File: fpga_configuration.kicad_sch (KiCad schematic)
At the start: 53 parts, among them IC1 ECP5-BGA256, J10 TC_SWD, J6 MCU_SWD, U6 ATSAMD11, U7 W25Q32JVSS

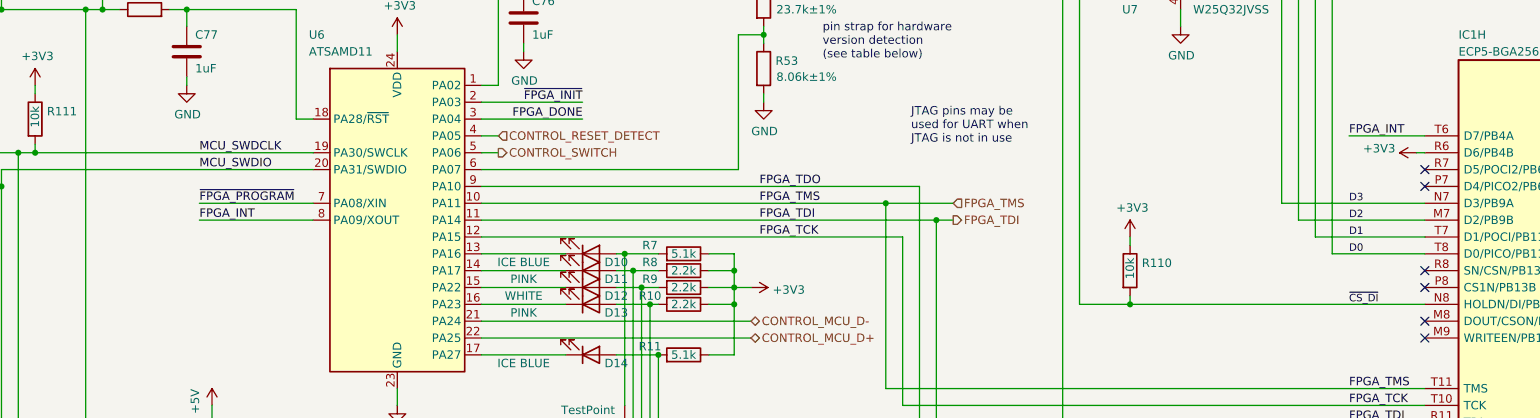
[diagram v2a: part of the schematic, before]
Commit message: Rename FPGA_INT to FPGA_ADV
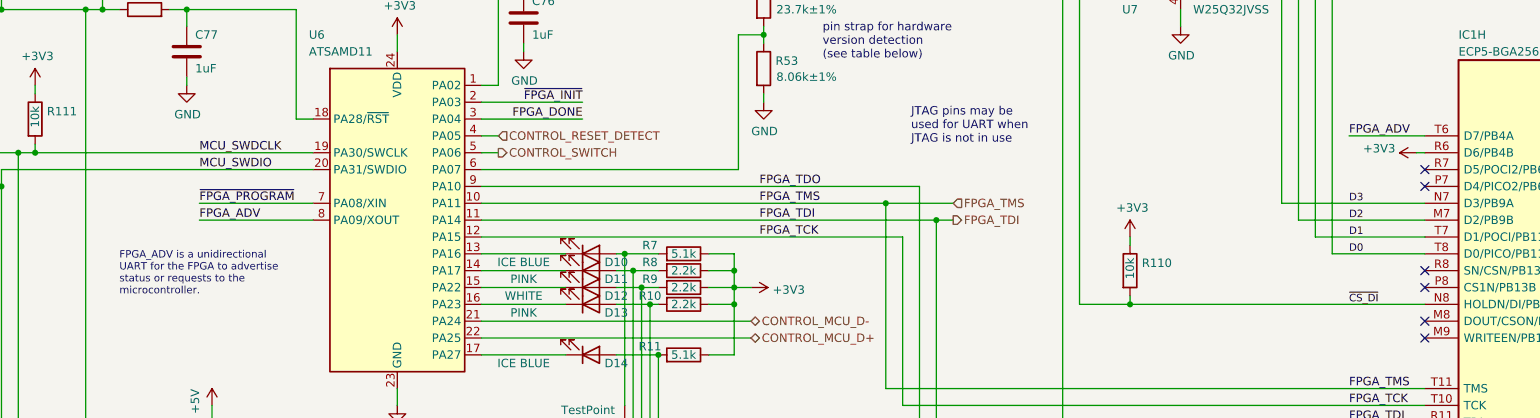
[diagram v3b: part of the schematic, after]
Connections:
- net FPGA_INT renamed FPGA_ADV
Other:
- note added: "FPGA_ADV is a unidirectional UART for the FPGA to advertise status or requests to the microcontroller."
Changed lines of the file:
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@@
     (effects (font (size 1.27 1.27)) (justify left bottom))
+  )
+  (text "FPGA_ADV is a unidirectional\nUART for the FPGA to advertise\nstatus or requests to the\nmicrocontroller."
+    (at 50.8 91.44 0)
+    (effects (font (size 1.1176 1.1176)) (justify left bottom))
   )
   (text "1.2" (at 135.89 182.88 0)
@@
     (effects (font (size 1.27 1.27)) (justify right bottom))
   )
-  (label "FPGA_INT" (at 236.22 67.31 0)
+  (label "FPGA_ADV" (at 236.22 67.31 0)
     (effects (font (size 1.27 1.27)) (justify left bottom))
   )
@@
     (effects (font (size 1.27 1.27)) (justify left bottom))
   )
-  (label "FPGA_INT" (at 62.865 80.01 0)
+  (label "FPGA_ADV" (at 62.865 80.01 0)
     (effects (font (size 1.27 1.27)) (justify left bottom))
   )

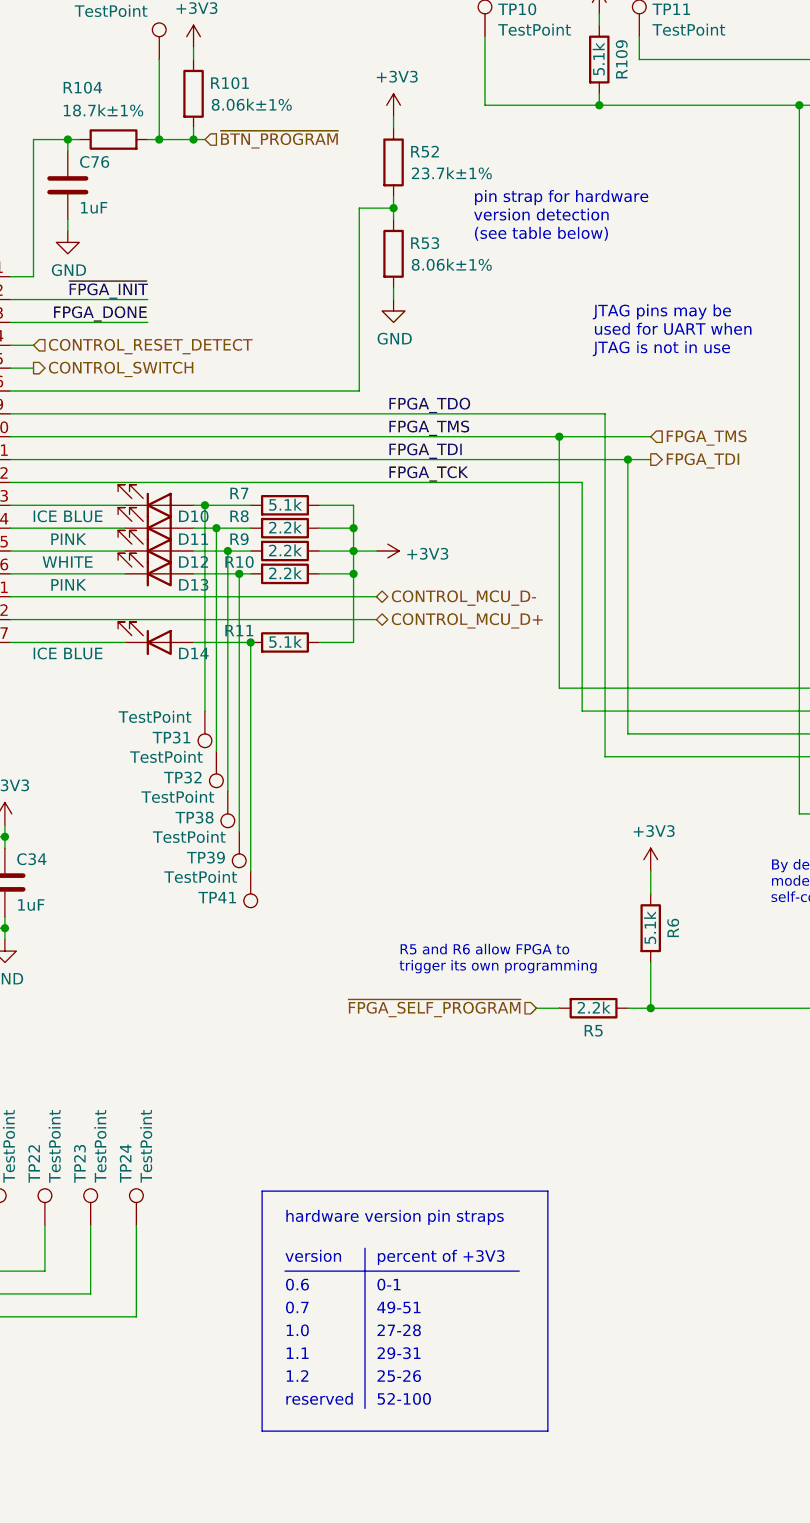
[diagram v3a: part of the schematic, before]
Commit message: Update version detection pin strap
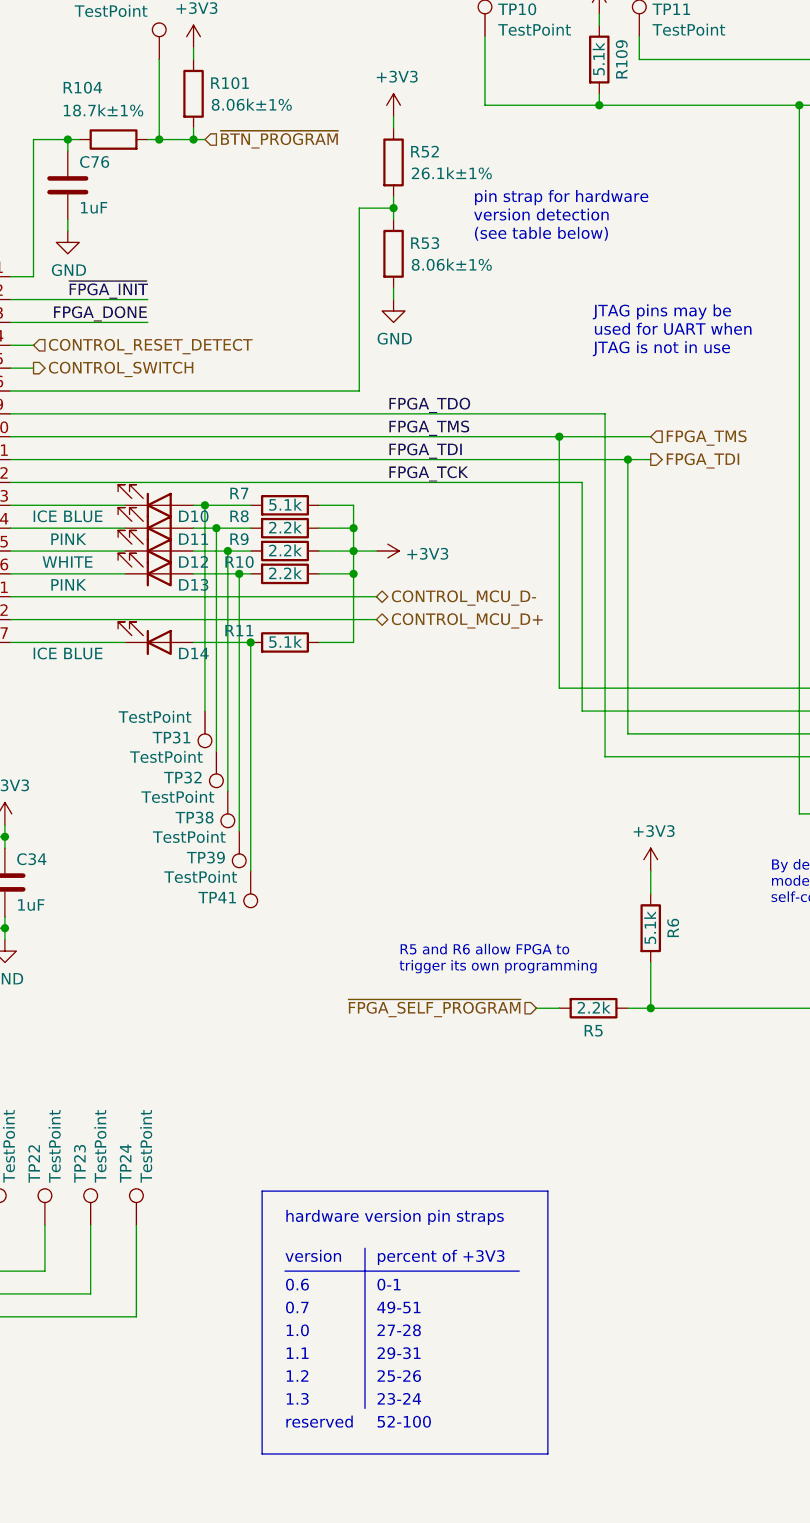
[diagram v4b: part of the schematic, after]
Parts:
- R52: value 23.7k±1% -> 26.1k±1%; Part Number RC0402FR-0723K7L -> RC0402FR-0726K1L
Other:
- note added: "1.3"
- note added: "23-24"
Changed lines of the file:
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@@
     (stroke (width 0) (type default) (color 0 0 0 0))
   )
-  (polyline (pts (xy 133.35 161.29) (xy 133.35 187.96))
+  (polyline (pts (xy 133.35 161.29) (xy 133.35 190.5))
     (stroke (width 0) (type default) (color 0 0 0 0))
   )
@@
     (stroke (width 0) (type default) (color 0 0 0 0))
   )
-  (polyline (pts (xy 165.1 161.29) (xy 165.1 187.96))
+  (polyline (pts (xy 165.1 161.29) (xy 165.1 190.5))
     (stroke (width 0) (type default) (color 0 0 0 0))
   )
@@
     (stroke (width 0) (type default) (color 0 0 0 0))
   )
-  (polyline (pts (xy 165.1 187.96) (xy 133.35 187.96))
+  (polyline (pts (xy 165.1 190.5) (xy 133.35 190.5))
     (stroke (width 0) (type default) (color 0 0 0 0))
   )
@@
     (effects (font (size 3.5052 3.5052)) (justify left bottom))
   )
-  (text "reserved" (at 135.89 185.42 0)
+  (text "reserved" (at 135.89 187.96 0)
     (effects (font (size 1.27 1.27)) (justify left bottom))
   )
@@
     (effects (font (size 1.1176 1.1176)) (justify left bottom))
   )
-  (text "52-100" (at 146.05 185.42 0)
+  (text "52-100" (at 146.05 187.96 0)
     (effects (font (size 1.27 1.27)) (justify left bottom))
   )
@@
   )
   (text "1.0" (at 135.89 177.8 0)
+    (effects (font (size 1.27 1.27)) (justify left bottom))
+  )
+  (text "23-24" (at 146.05 185.42 0)
     (effects (font (size 1.27 1.27)) (justify left bottom))
   )
@@
   )
   (text "0.7" (at 135.89 175.26 0)
+    (effects (font (size 1.27 1.27)) (justify left bottom))
+  )
+  (text "1.3" (at 135.89 185.42 0)
     (effects (font (size 1.27 1.27)) (justify left bottom))
   )
@@
       (effects (font (size 1.27 1.27)) (justify left))
     )
-    (property "Value" "23.7k±1%" (id 1) (at 149.86 48.26 0)
+    (property "Value" "26.1k±1%" (id 1) (at 149.86 48.26 0)
       (effects (font (size 1.27 1.27)) (justify left))
     )
@@
       (effects (font (size 1.27 1.27)) hide)
     )
-    (property "Part Number" "RC0402FR-0723K7L" (id 4) (at 147.955 46.99 0)
+    (property "Part Number" "RC0402FR-0726K1L" (id 4) (at 147.955 46.99 0)
       (effects (font (size 1.27 1.27)) hide)
     )
@@
       (effects (font (size 1.27 1.27)) hide)
     )
-    (property "Description" "RES 23.7K OHM 1% 1/16W 0402" (id 7) (at 147.955 46.99 0)
-      (effects (font (size 1.27 1.27)) hide)
-    )
+    (property "Description" "RES 26.1K OHM 1% 1/16W 0402" (id 7) (at 147.955 46.99 0)
+      (effects (font (size 1.27 1.27)) hide)
+    )
